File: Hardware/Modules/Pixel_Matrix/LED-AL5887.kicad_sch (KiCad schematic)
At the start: 46 parts, among them J1 B4B-EH-A, J2 Conn_01x03_Pin, J3 Conn_01x03_Pin, J4 Conn_01x03_Pin, J5 B6B-EH-A, U1 AL5887JAZW52-13

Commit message: Pin 51 gefixt
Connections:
- net GND: no longer U1.51 (~{EN})
- net at J2.1 (Pin_1), J3.1 (Pin_1), J4.1 (Pin_1)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: now also U1.51 (~{EN})
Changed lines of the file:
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@@
+	)
+	(junction
+		(at 46.99 40.64)
+		(diameter 0)
+		(color 0 0 0 0)
 	)
 	(junction
@@
 	)
 	(junction
-		(at 48.26 36.83)
-		(diameter 0)
-		(color 0 0 0 0)
-	)
-	(junction
 		(at 130.81 123.19)
 		(diameter 0)
@@
 	(wire
 		(pts
-			(xy 46.99 19.05) (xy 46.99 99.06)
+			(xy 46.99 19.05) (xy 46.99 40.64)
 		)
 		(stroke
@@
 	(wire
 		(pts
+			(xy 46.99 40.64) (xy 46.99 99.06)
+		)
+		(stroke
+			(width 0)
+			(type default)
+		)
+	)
+	(wire
+		(pts
 			(xy 130.81 132.08) (xy 130.81 130.81)
 		)
@@
 	(wire
 		(pts
-			(xy 45.72 44.45) (xy 45.72 20.32)
+			(xy 45.72 20.32) (xy 45.72 44.45)
 		)
 		(stroke
@@
 	(wire
 		(pts
-			(xy 50.8 36.83) (xy 48.26 36.83)
-		)
-		(stroke
-			(width 0)
-			(type default)
-		)
-	)
-	(wire
-		(pts
 			(xy 134.62 118.11) (xy 121.92 118.11)
 		)
@@
 	(wire
 		(pts
-			(xy 50.8 40.64) (xy 50.8 36.83)
-		)
-		(stroke
-			(width 0)
-			(type default)
-		)
-	)
-	(wire
-		(pts
 			(xy 26.67 78.74) (xy 30.48 78.74)
 		)
@@
 		)
 		(stroke
+			(width 0)
+			(type default)
+		)
+	)
+	(wire
+		(pts
+			(xy 46.99 40.64) (xy 50.8 40.64)
+		)
+		(stroke

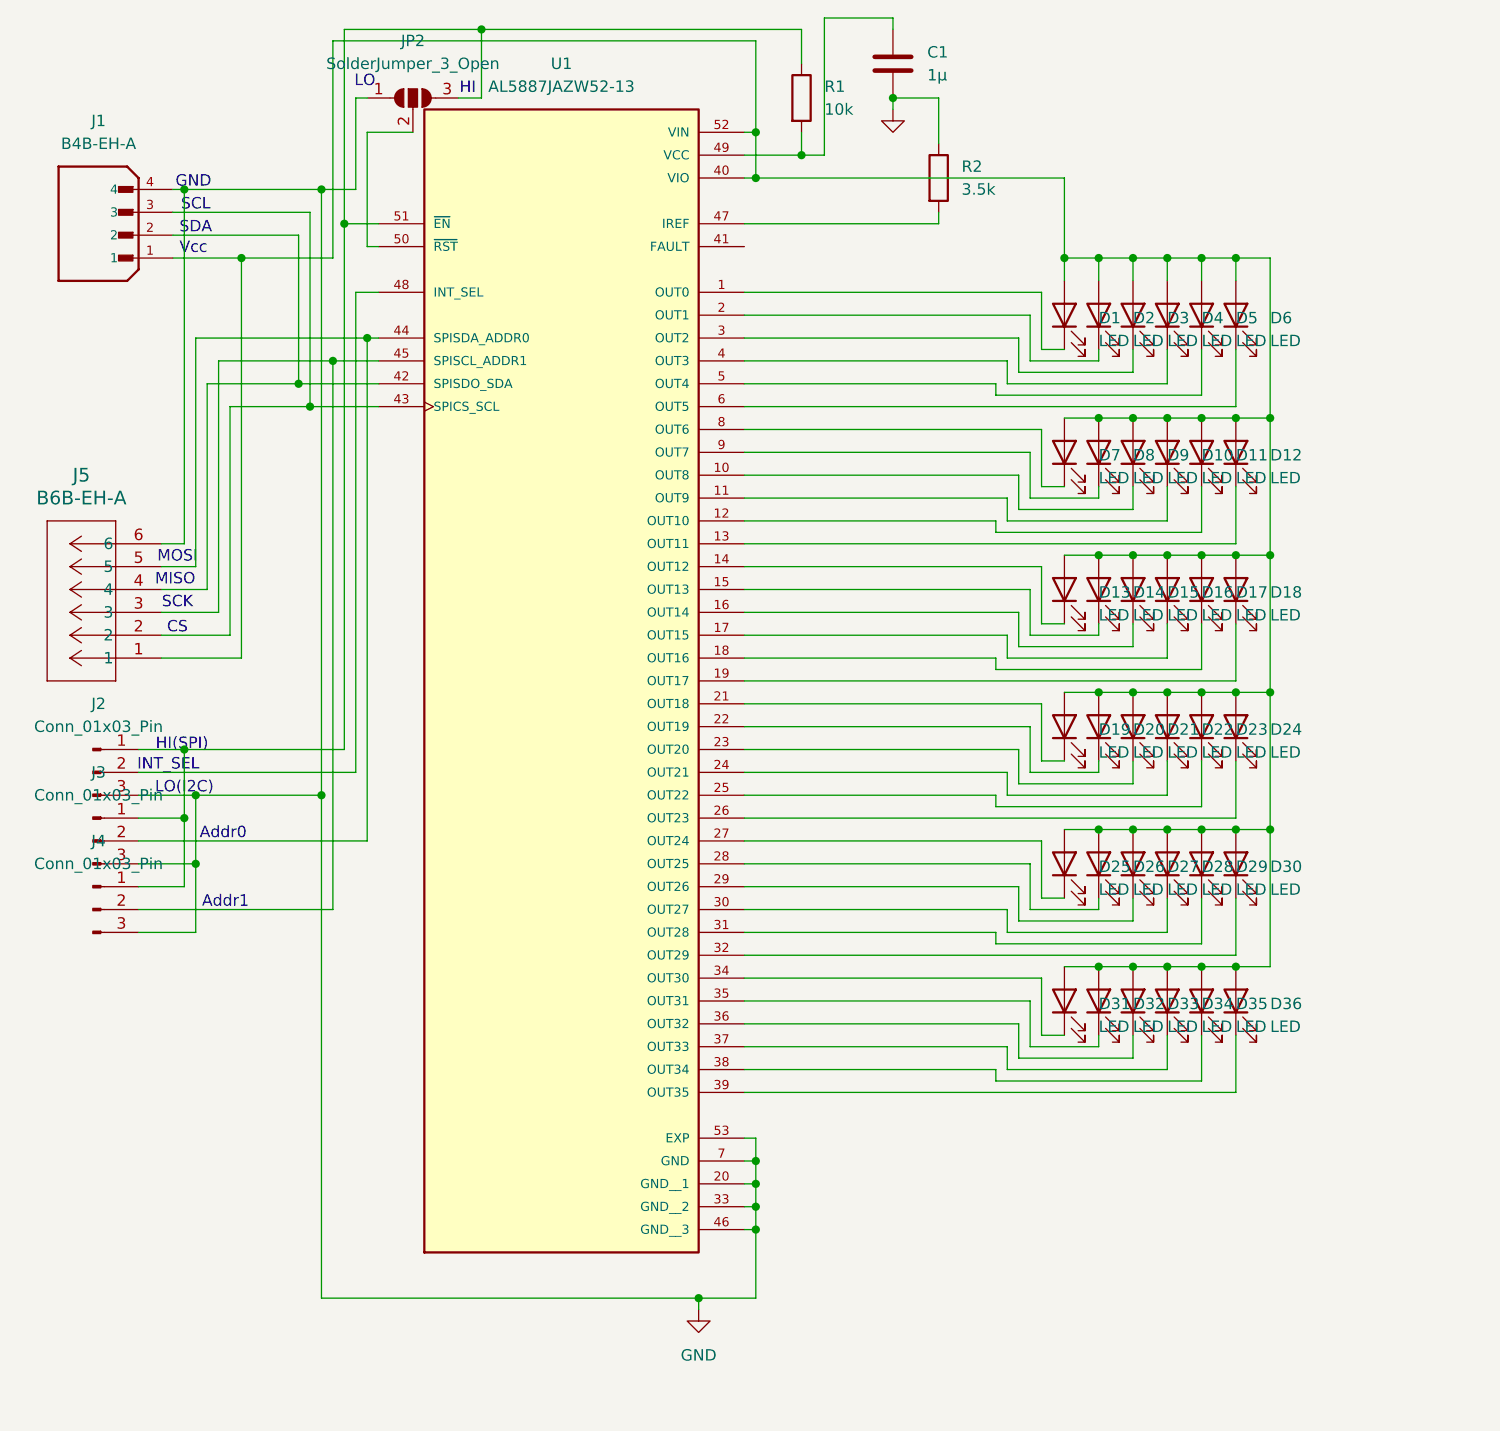
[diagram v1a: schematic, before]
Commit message: Fixed Pixel matrix
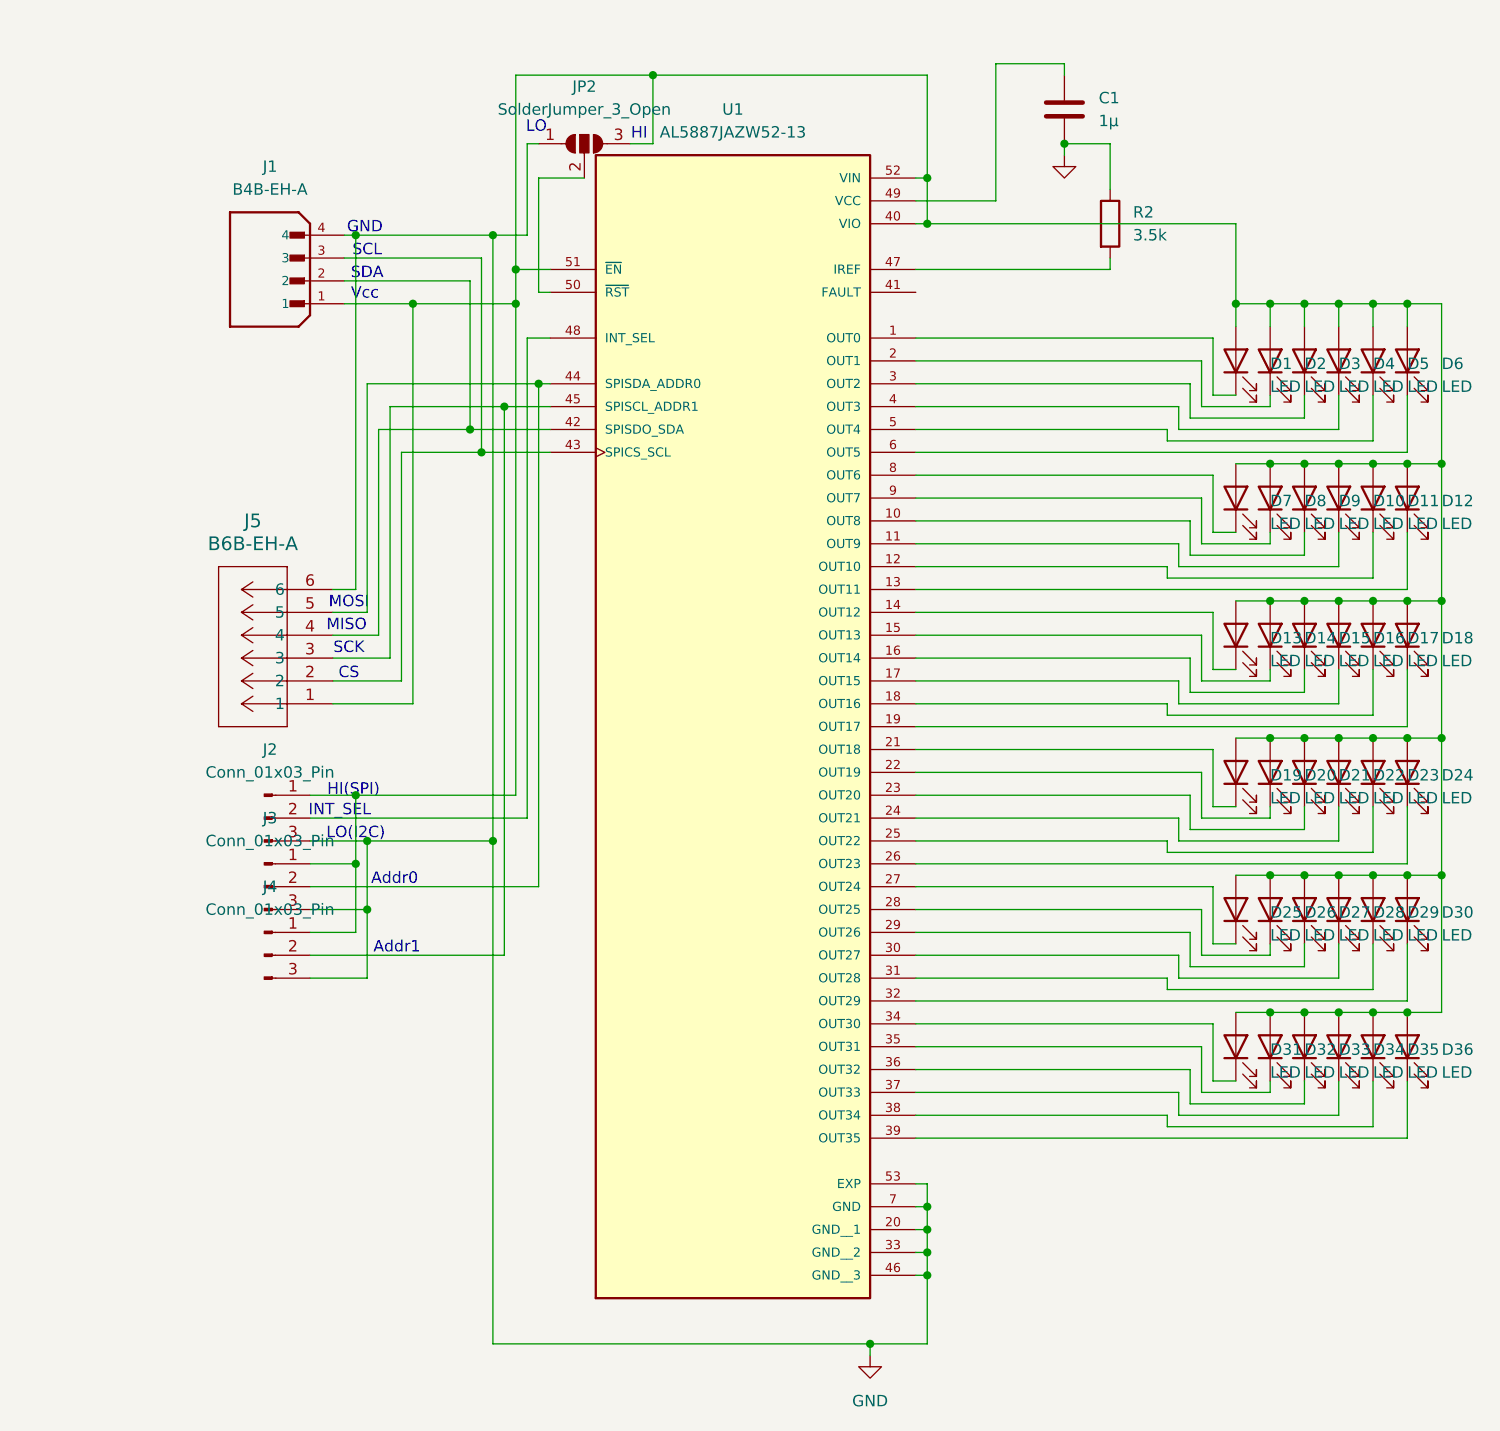
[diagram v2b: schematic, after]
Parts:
- removed R1: 10k, Resistor_SMD:R_0603_1608Metric_Pad0.98x0.95mm_HandSolder, symbol Device:R
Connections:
- net at J2.1 (Pin_1), J3.1 (Pin_1), J4.1 (Pin_1)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: now also D1.2 (A), D10.2 (A), D11.2 (A), D12.2 (A), D13.2 (A), D14.2 (A), D15.2 (A), D16.2 (A), D17.2 (A), D18.2 (A), D19.2 (A), D2.2 (A), D20.2 (A), D21.2 (A), D22.2 (A), D23.2 (A), D24.2 (A), D25.2 (A), D26.2 (A), D27.2 (A), D28.2 (A), D29.2 (A), D3.2 (A), D30.2 (A), D31.2 (A), D32.2 (A), D33.2 (A), D34.2 (A), D35.2 (A), D36.2 (A), D4.2 (A), D5.2 (A), D6.2 (A), D7.2 (A), D8.2 (A), D9.2 (A), J1.1, J5.1, U1.40 (VIO), U1.52 (VIN)
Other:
- moved on the sheet: C1, D1, D10, D11, D12, D13, D14, D15, D16, D17, D18, D19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
